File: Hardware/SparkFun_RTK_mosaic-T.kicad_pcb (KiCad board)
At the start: 4 copper layers, 151.8 x 101.6 mm, 261 parts, among them J1 SMA_Edge, J11 SMA_Edge, J12 SMA_Edge, J2 USB_C_Receptacle, J3 U.FL, J4 USB_C_Receptacle, J5 MagJack_PoE, J6 microSD, J7 Qwiic_Vertical, J8 RP-SMA_Edge, J9 Screw_Cage_3.5mm-10, Q1 MBT3904DW1, SW1 PTH_RA_h7.5mm, SW2 PTH_RA_h7.5mm, SW3 PTH_RA_h7.5mm, SW4 SPDT_Slide_SMD_7.2x3.5mm, U1 ESP32-WROVER-IE-N16R8, U10 74LVC2T45DC, U11 AP2112K-3.3, U12 74LVC2T45DC, U13 SiT5358AI-FS033IT-10.000000, U14 74LVC2T45DC, U15 74LVC2T45DC, U16 74LVC2T45DC, U2 mosaic-X5, U3 CH340C, U4 KSZ8041NL/I, U5 AP2112K-3.3, U6 REC15E-2405SZ, U7 Ag9905M, U8 74LVC2T45DC, U9 74LVC2T45DC

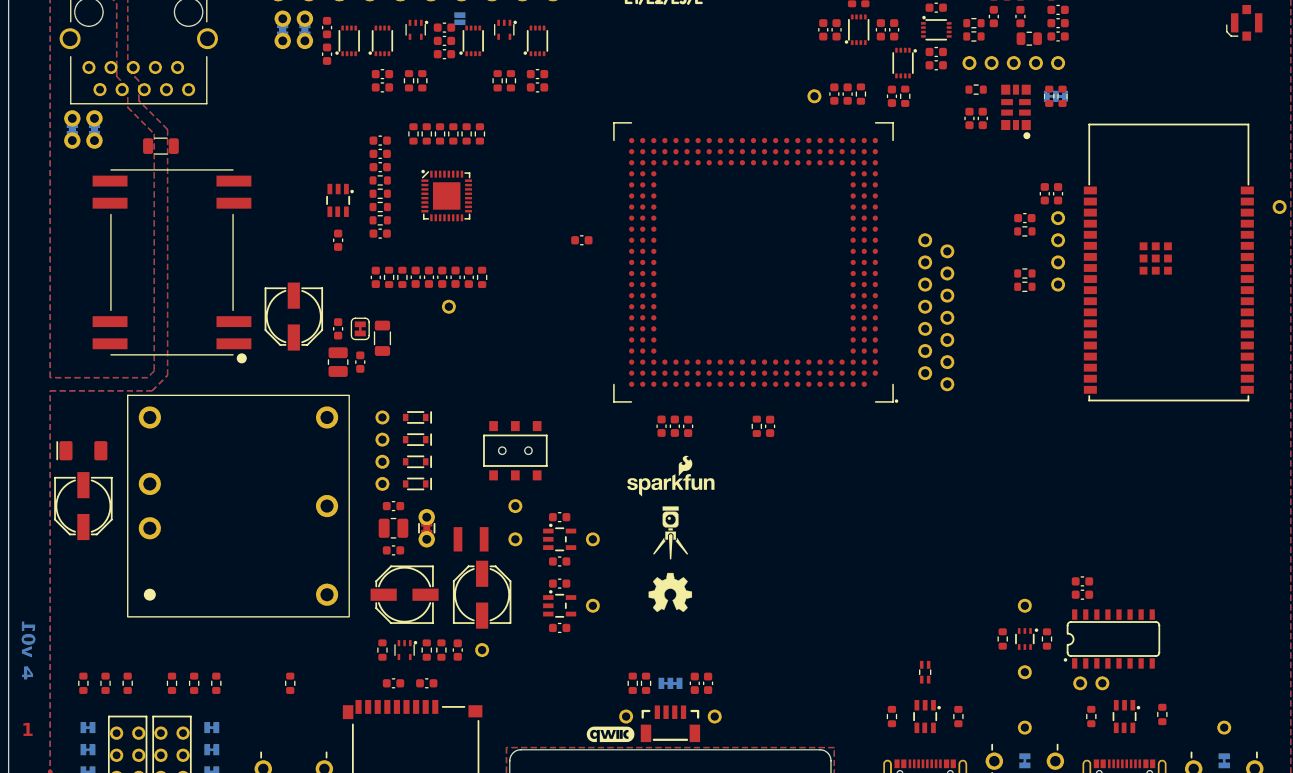
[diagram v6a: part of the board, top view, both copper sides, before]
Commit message: Add more silk
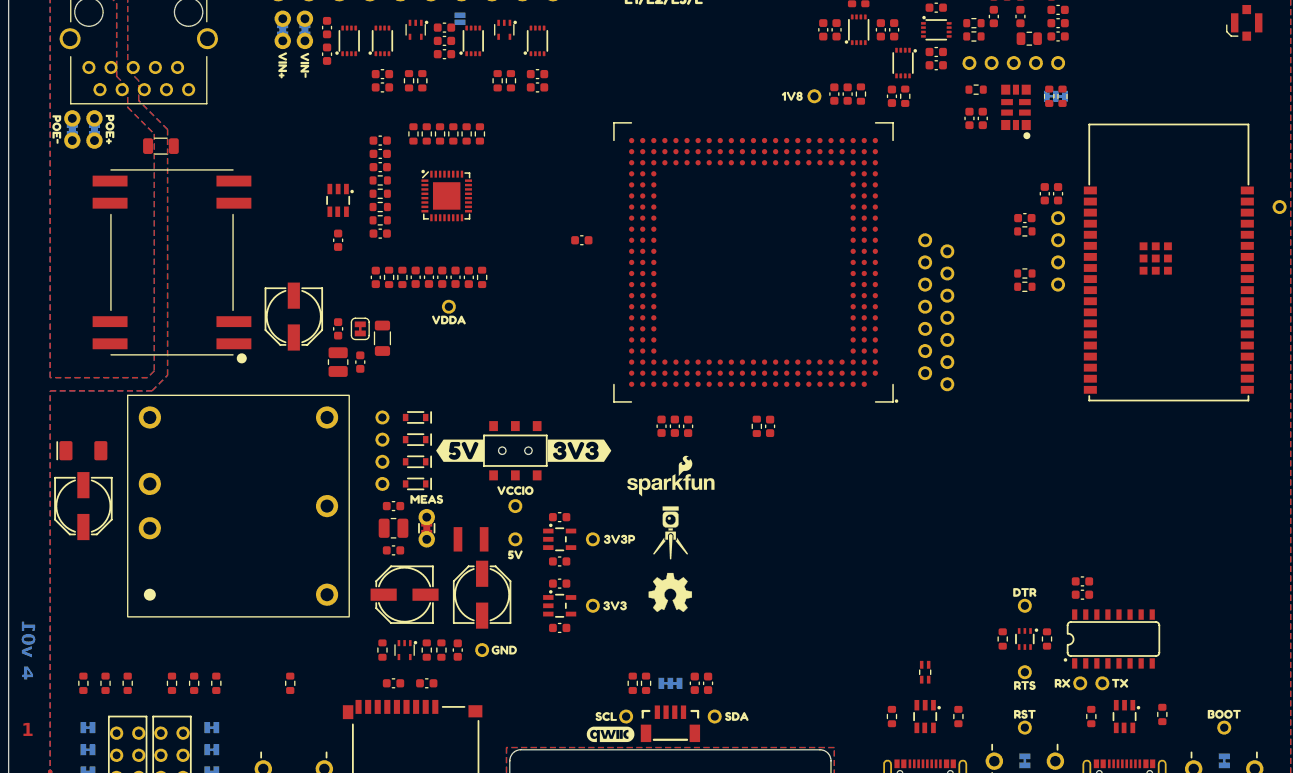
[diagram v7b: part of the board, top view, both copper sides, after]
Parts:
- added kibuzzard-65A7F440: G***, kibuzzard-65A7F440, F.Cu at (158.8, 133.3)
- added kibuzzard-65A7F511: G***, kibuzzard-65A7F511, F.Cu at (171.4, 128.3)
- added kibuzzard-65A7F548: G***, kibuzzard-65A7F548, F.Cu at (172.0, 120.7)
- added kibuzzard-65A7F771: G***, kibuzzard-65A7F771, F.Cu at (191.8, 69.8)
- added kibuzzard-66A11DB0: G***, kibuzzard-66A11DB0, B.Cu at (204.5, 94.0)
- added kibuzzard-66A11DCF: G***, kibuzzard-66A11DCF, B.Cu at (204.5, 91.4)
- added kibuzzard-66A11DE1: G***, kibuzzard-66A11DE1, B.Cu at (212.3, 100.3)
- added kibuzzard-66A11DF6: G***, kibuzzard-66A11DF6, B.Cu at (212.6, 102.9)
- added kibuzzard-66A11E07: G***, kibuzzard-66A11E07, B.Cu at (212.3, 95.2)
- added kibuzzard-66A11E14: G***, kibuzzard-66A11E14, B.Cu at (212.3, 92.7)
- added kibuzzard-66A11E22: G***, kibuzzard-66A11E22, B.Cu at (212.3, 90.2)
- added kibuzzard-66A11E31: G***, kibuzzard-66A11E31, B.Cu at (204.0, 88.9)
- added kibuzzard-66A11E3D: G***, kibuzzard-66A11E3D, B.Cu at (212.6, 87.6)
- added kibuzzard-66A11E48: G***, kibuzzard-66A11E48, B.Cu at (204.5, 86.4)
- added kibuzzard-66A11E61: G***, kibuzzard-66A11E61, B.Cu at (220.2, 86.4)
- added kibuzzard-66A11E6E: G***, kibuzzard-66A11E6E, B.Cu at (220.2, 88.9)
- added kibuzzard-66A11E7B: G***, kibuzzard-66A11E7B, B.Cu at (220.2, 91.4)
- added kibuzzard-66A11E89: G***, kibuzzard-66A11E89, B.Cu at (245.6, 82.5)
- added kibuzzard-66A11EB6: G***, kibuzzard-66A11EB6, B.Cu at (212.1, 62.7)
- added kibuzzard-66A11ECA: G***, kibuzzard-66A11ECA, B.Cu at (214.6, 63.2)
- added kibuzzard-66A11ED7: G***, kibuzzard-66A11ED7, B.Cu at (217.2, 63.5)
- added kibuzzard-66A11EE6: G***, kibuzzard-66A11EE6, B.Cu at (219.7, 63.2)
- added kibuzzard-66A11EF1: G***, kibuzzard-66A11EF1, B.Cu at (222.2, 63.2)
- added kibuzzard-66A11F21: G***, kibuzzard-66A11F21, F.Cu at (160.0, 122.4)
- added kibuzzard-66A11F21: G***, kibuzzard-66A11F21, B.Cu at (160.0, 122.4)
- added kibuzzard-66A11F39: G***, kibuzzard-66A11F39, F.Cu at (160.0, 115.1)
- added kibuzzard-66A11F39: G***, kibuzzard-66A11F39, B.Cu at (160.0, 115.1)
- added kibuzzard-66A11F9C: G***, kibuzzard-66A11F9C, F.Cu at (167.4, 110.5)
- added kibuzzard-66A11FB3: G***, kibuzzard-66A11FB3, F.Cu at (153.7, 110.5)
- added kibuzzard-66A11FEE: G***, kibuzzard-66A11FEE, F.Cu at (149.9, 116.1)
- added kibuzzard-66A11FEE: G***, kibuzzard-66A11FEE, B.Cu at (149.9, 116.1)
- added kibuzzard-66A12010: G***, kibuzzard-66A12010, B.Cu at (142.2, 106.7)
- added kibuzzard-66A1201E: G***, kibuzzard-66A1201E, B.Cu at (141.5, 109.2)
- added kibuzzard-66A12027: G***, kibuzzard-66A12027, B.Cu at (142.0, 111.8)
- added kibuzzard-66A12034: G***, kibuzzard-66A12034, B.Cu at (142.0, 114.3)
- added kibuzzard-66A12099: G***, kibuzzard-66A12099, B.Cu at (128.3, 142.2)
- added kibuzzard-66A120AA: G***, kibuzzard-66A120AA, B.Cu at (128.3, 144.8)
- added kibuzzard-66A120EB: G***, kibuzzard-66A120EB, B.Cu at (128.2, 147.3)
- added kibuzzard-66A12140: G***, kibuzzard-66A12140, B.Cu at (107.2, 142.2)
- added kibuzzard-66A12152: G***, kibuzzard-66A12152, B.Cu at (107.7, 144.8)
- added kibuzzard-66A12161: G***, kibuzzard-66A12161, B.Cu at (111.0, 148.8)
- added kibuzzard-66A12184: G***, kibuzzard-66A12184, F.Cu at (170.4, 141.0)
- added kibuzzard-66A12184: G***, kibuzzard-66A12184, B.Cu at (170.4, 141.0)
- added kibuzzard-66A12197: G***, kibuzzard-66A12197, F.Cu at (185.4, 141.0)
- added kibuzzard-66A12197: G***, kibuzzard-66A12197, B.Cu at (185.4, 141.0)
- added kibuzzard-66A121BE: G***, kibuzzard-66A121BE, F.Cu at (218.4, 140.7)
- added kibuzzard-66A121BE: G***, kibuzzard-66A121BE, B.Cu at (218.4, 140.7)
- added kibuzzard-66A121D2: G***, kibuzzard-66A121D2, F.Cu at (218.4, 137.4)
- added kibuzzard-66A121D2: G***, kibuzzard-66A121D2, B.Cu at (218.4, 137.4)
- added kibuzzard-66A1223B: G***, kibuzzard-66A1223B, F.Cu at (222.8, 137.2)
- added kibuzzard-66A1223B: G***, kibuzzard-66A1223B, B.Cu at (222.8, 137.2)
- added kibuzzard-66A12248: G***, kibuzzard-66A12248, F.Cu at (229.4, 137.2)
- added kibuzzard-66A12248: G***, kibuzzard-66A12248, B.Cu at (229.4, 137.2)
- added kibuzzard-66A12259: G***, kibuzzard-66A12259, F.Cu at (218.4, 126.7)
- added kibuzzard-66A12259: G***, kibuzzard-66A12259, B.Cu at (218.4, 126.7)
- added kibuzzard-66A12273: G***, kibuzzard-66A12273, F.Cu at (241.3, 140.7)
- added kibuzzard-66A12273: G***, kibuzzard-66A12273, B.Cu at (241.3, 140.7)
- added kibuzzard-66A122A4: G***, kibuzzard-66A122A4, F.Cu at (152.4, 95.5)
- added kibuzzard-66A122A4: G***, kibuzzard-66A122A4, B.Cu at (152.4, 95.5)
- added kibuzzard-66A122D2: G***, kibuzzard-66A122D2, F.Cu at (133.3, 66.3)
- added kibuzzard-66A122D2: G***, kibuzzard-66A122D2, B.Cu at (133.3, 66.3)
- added kibuzzard-66A12315: G***, kibuzzard-66A12315, F.Cu at (135.9, 66.3)
- added kibuzzard-66A12315: G***, kibuzzard-66A12315, B.Cu at (135.9, 66.3)
- added kibuzzard-66A12334: G***, kibuzzard-66A12334, F.Cu at (113.5, 73.7)
- added kibuzzard-66A12334: G***, kibuzzard-66A12334, B.Cu at (113.5, 73.7)
- added kibuzzard-66A12372: G***, kibuzzard-66A12372, F.Cu at (107.4, 73.7)
- added kibuzzard-66A12372: G***, kibuzzard-66A12372, B.Cu at (107.4, 73.7)
